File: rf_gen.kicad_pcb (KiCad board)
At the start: 2 copper layers, 101.6 x 35.7 mm, 52 parts, among them J1 Conn_01x07_Male, J2 Screw_Terminal_01x04, J3 Conn_01x05_Male, Q1 GS61004B, Q2 G3R350MT12J, U1 NPC81074, U2 AP62150

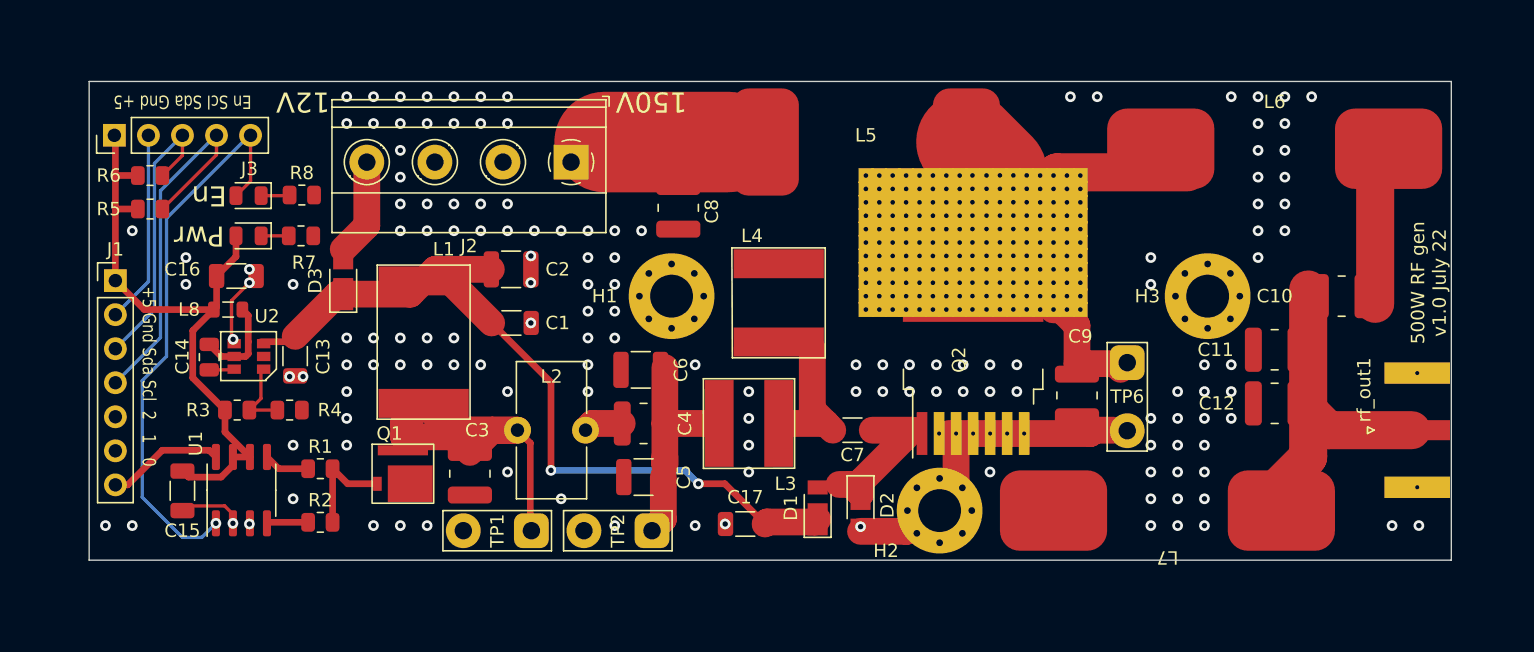
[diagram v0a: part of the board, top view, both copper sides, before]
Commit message: Added heatsink, improved eq core windings
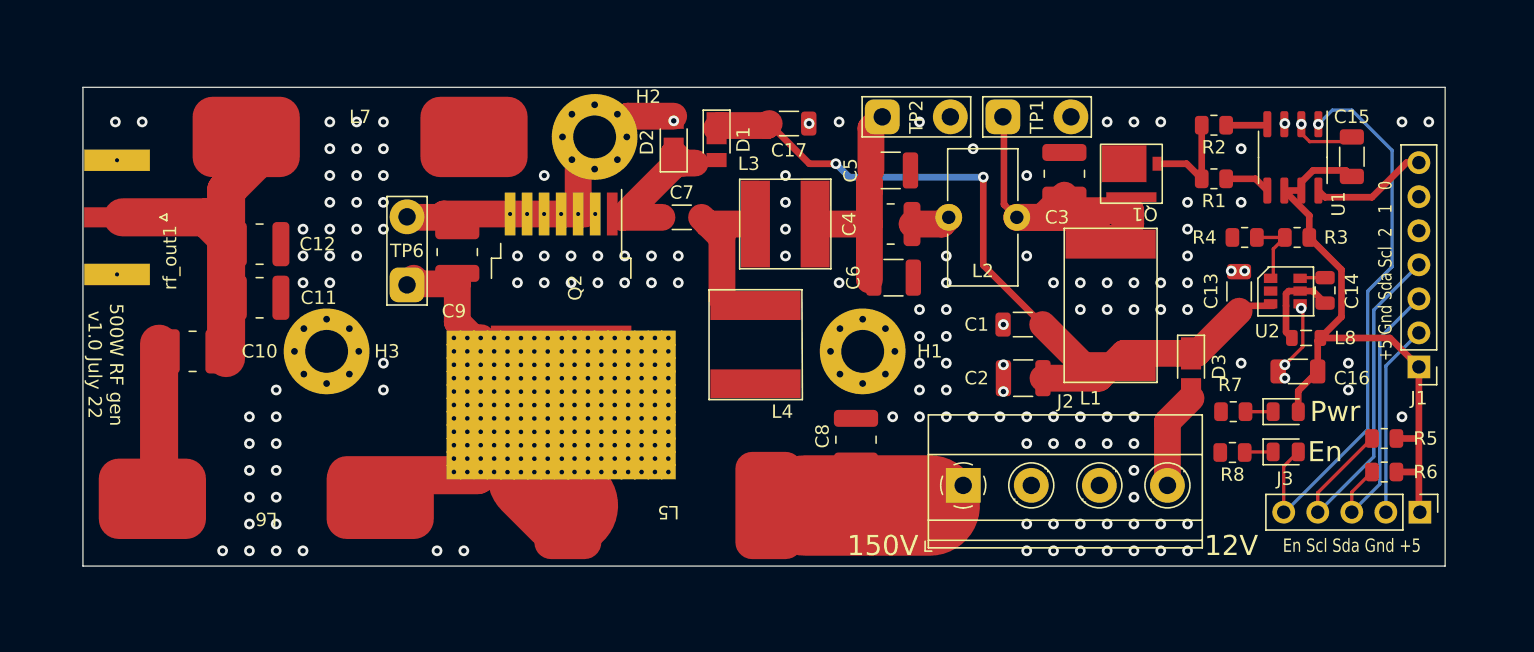
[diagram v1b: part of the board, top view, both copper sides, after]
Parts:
- added REF**: heatsink_45x45, rf_gen:heatsink_45x45, B.Cu at (106.3, 122.1)
- moved J3 101.4 mm to (168.3, 136.1), turned to -90 degrees
- moved rf_out1 98.3 mm to (71.1, 114.1), turned to 180 degrees
- moved J1 97.5 mm to (168.3, 125.3), turned to 180 degrees
- moved R6 94.7 mm to (165.7, 133.1), turned to 180 degrees
- moved R5 93.7 mm to (165.7, 130.6), turned to 0 degrees
- moved C15 90.8 mm to (163.3, 109.6), turned to 90 degrees
- moved C10 85.8 mm to (76.8, 124.1), turned to 0 degrees
- moved C14 83.4 mm to (161.3, 119.6), turned to -90 degrees
- moved U1 82.3 mm to (158.9, 109.6), turned to -90 degrees
- moved L6 81.0 mm to (82.3, 136.1), turned to 180 degrees
- moved L8 80.5 mm to (159.8, 123.1), turned to 0 degrees
- moved R3 80.1 mm to (159.2, 115.6), turned to 180 degrees
- moved D5 79.7 mm to (158.3, 131.6), turned to 0 degrees
- moved C16 79.5 mm to (159.2, 125.6), turned to 180 degrees
- moved D4 78.5 mm to (158.3, 128.6), turned to 0 degrees
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
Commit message: Added 3d model for toroid inductor
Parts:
- L2: footprint Inductor_THT:L_Toroid_Vertical_L10.0mm_W5.0mm_P5.08mm -> rf_gen:L_Toroid_Vertical_L10.0mm_W5.0mm_P5.08mm
- turned REF** to 45 degrees
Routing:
- net GND: track 48.2 -> 42.7 mm, vias 145 -> 142
- net Net-(C14-Pad1): track 1.86 -> 5.53 mm, vias 0 -> 3
- net Net-(R3-Pad2): track 5.34 -> 7.21 mm

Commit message: Fixed DRC issues
Buck regulator was wired incorrectly. Not sure how this happened.
Increased spacing between pads on RF capacitor to reduce chance of arcing
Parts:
- moved C10 0.76 mm to (76.0, 124.1)
- moved U2 0.47 mm to (158.2, 120.0)
- moved C14 0.43 mm to (161.3, 120.0)
- moved C13 0.36 mm to (154.8, 120.0), turned to -90 degrees
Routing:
- net GND: track 42.7 -> 50.0 mm, vias 142 -> 135
- net Net-(C10-Pad2): track 25.1 -> 28.7 mm
- net +12V: track 58.4 -> 61.8 mm
- net Net-(C14-Pad1): track 5.53 -> 3.21 mm, vias 3 -> 0
- net /SiC_gate: track 11.2 -> 12.8 mm
- net Net-(R3-Pad2): track 7.21 -> 5.96 mm
- net Net-(C14-Pad2): track 6.85 -> 7.96 mm
- net Net-(C9-Pad2): track 24.9 -> 24.3 mm
